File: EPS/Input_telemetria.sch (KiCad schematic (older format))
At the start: 21 parts

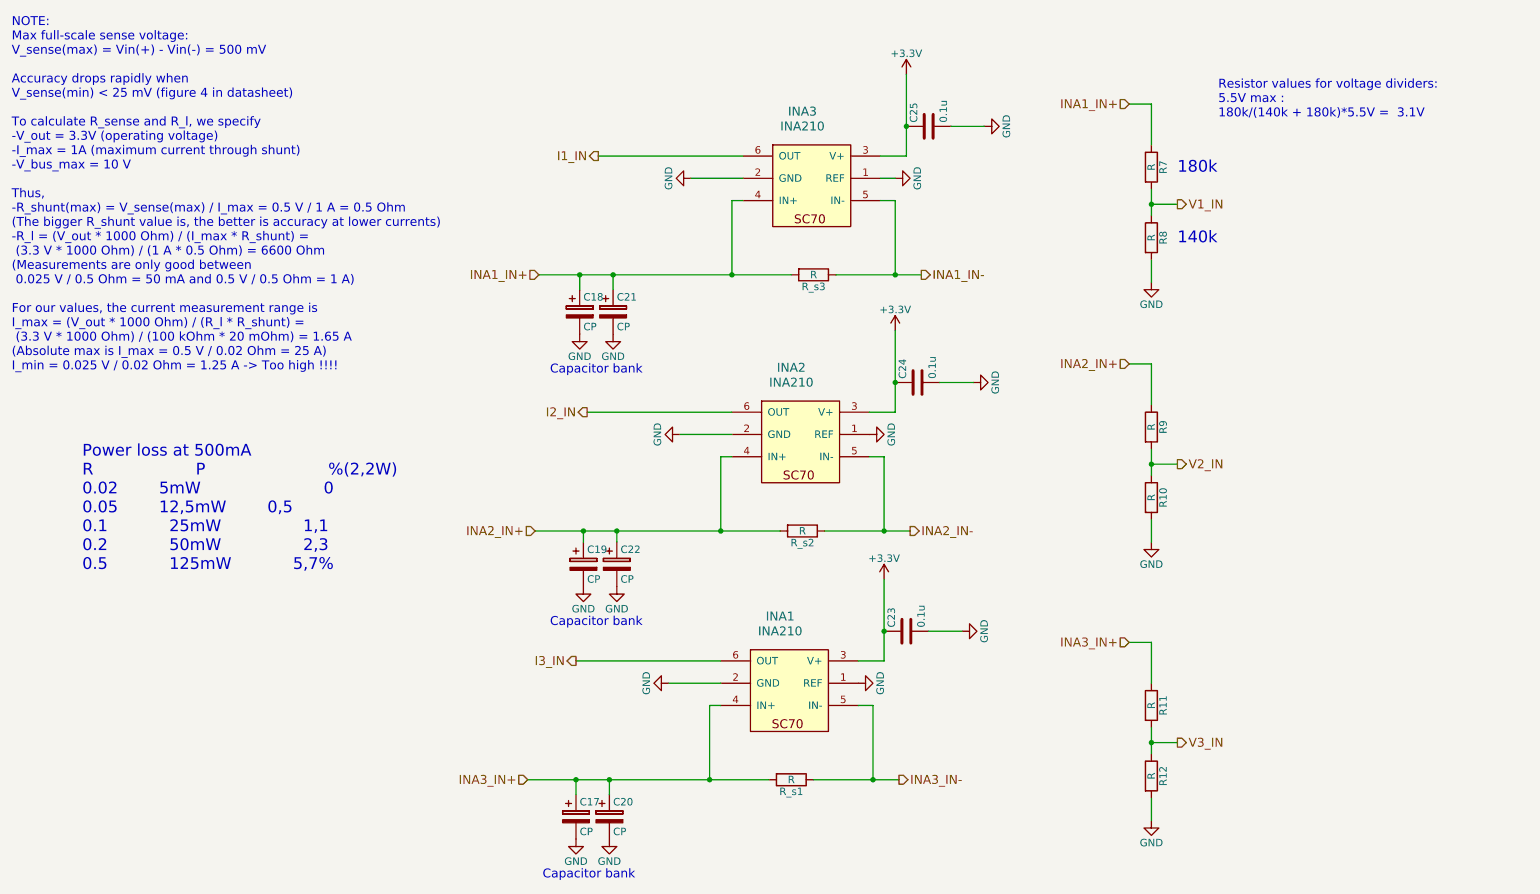
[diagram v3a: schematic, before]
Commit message: PCB updated
Added testpoints and updated PCB
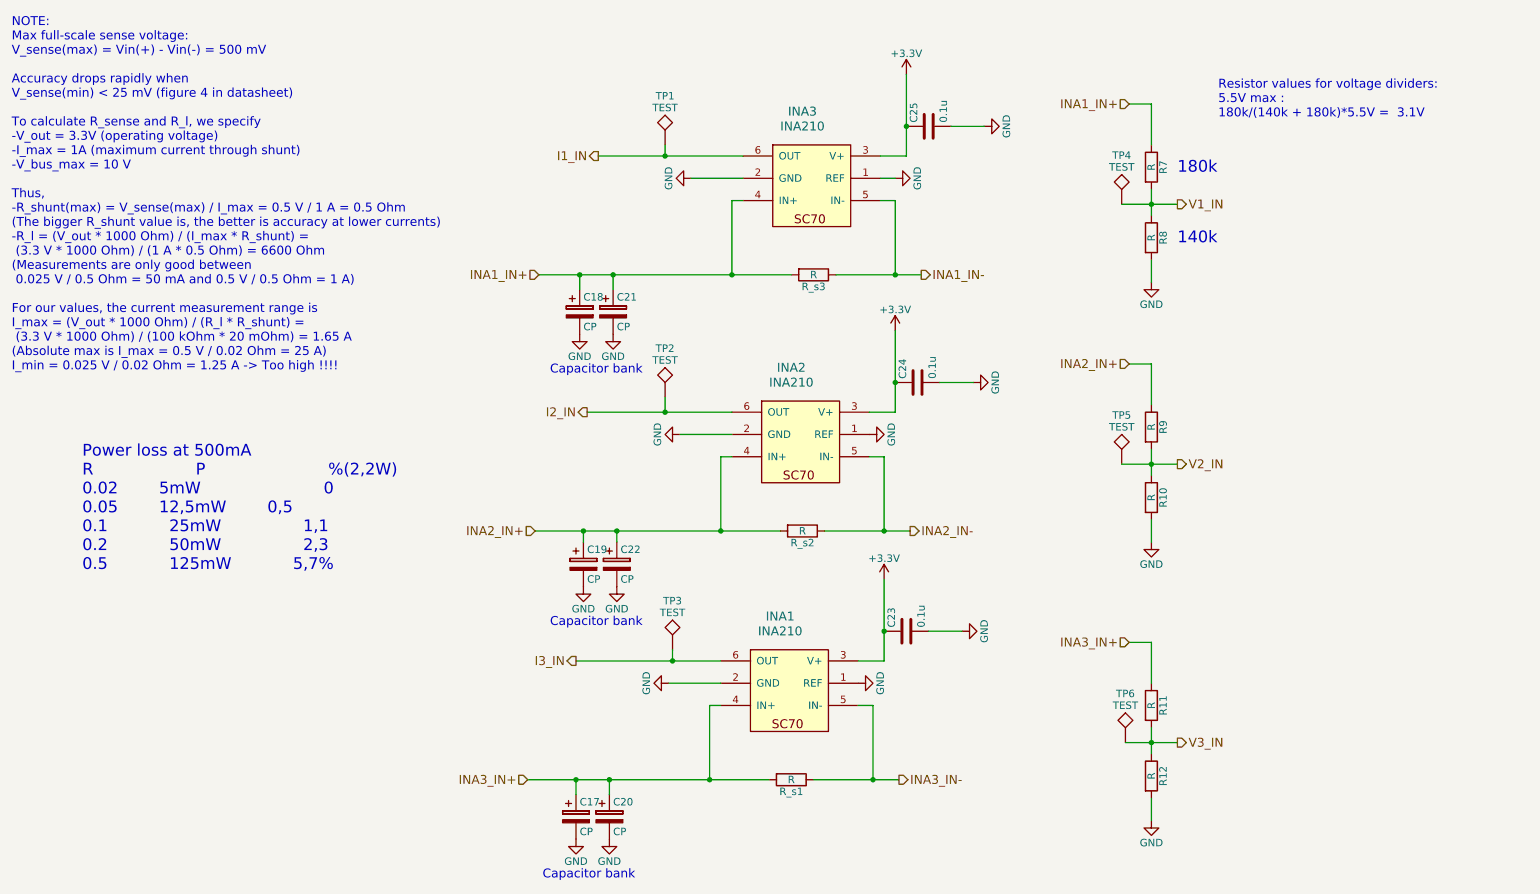
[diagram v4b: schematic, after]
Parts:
- added TP1, TP2, TP3, TP4, TP5, TP6: TEST, Measurement_Points:Measurement_Point_Round-SMD-Pad_Small, symbol TEST
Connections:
- net I1_IN: now also TP1.1
- net I2_IN: now also TP2.1
- net I3_IN: now also TP3.1
- net V1_IN: now also TP4.1
- net V2_IN: now also TP5.1
- net V3_IN: now also TP6.1
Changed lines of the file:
@@
 $EndComp
 $Comp
-L GND #PWR029
+L GND #PWR028
 U 1 1 5A8147F5
 P 5150 1650
-F 0 "#PWR029" H 5150 1400 50  0001 C CNN
+F 0 "#PWR028" H 5150 1400 50  0001 C CNN
 F 1 "GND" H 5150 1500 50  0000 C CNN
 F 2 "" H 5150 1650 50  0001 C CNN
@@
 $EndComp
 $Comp
-L +3.3V #PWR030
+L +3.3V #PWR029
 U 1 1 5A814819
 P 6600 950
-F 0 "#PWR030" H 6600 800 50  0001 C CNN
+F 0 "#PWR029" H 6600 800 50  0001 C CNN
 F 1 "+3.3V" H 6600 1090 50  0000 C CNN
 F 2 "" H 6600 950 50  0001 C CNN
@@
 Connection ~ 6600 1300
 $Comp
-L GND #PWR031
+L GND #PWR030
 U 1 1 5A814EB4
 P 7125 1300
-F 0 "#PWR031" H 7125 1050 50  0001 C CNN
+F 0 "#PWR030" H 7125 1050 50  0001 C CNN
 F 1 "GND" H 7125 1150 50  0000 C CNN
 F 2 "" H 7125 1300 50  0001 C CNN
@@
 $EndComp
 $Comp
-L GND #PWR032
+L GND #PWR031
 U 1 1 5A818451
 P 5075 3375
-F 0 "#PWR032" H 5075 3125 50  0001 C CNN
+F 0 "#PWR031" H 5075 3125 50  0001 C CNN
 F 1 "GND" H 5075 3225 50  0000 C CNN
 F 2 "" H 5075 3375 50  0001 C CNN
@@
 $EndComp
 $Comp
-L +3.3V #PWR033
+L +3.3V #PWR032
 U 1 1 5A818457
 P 6525 2675
-F 0 "#PWR033" H 6525 2525 50  0001 C CNN
+F 0 "#PWR032" H 6525 2525 50  0001 C CNN
 F 1 "+3.3V" H 6525 2815 50  0000 C CNN
 F 2 "" H 6525 2675 50  0001 C CNN
@@
 Connection ~ 6525 3025
 $Comp
-L GND #PWR034
+L GND #PWR033
 U 1 1 5A818460
 P 7050 3025
-F 0 "#PWR034" H 7050 2775 50  0001 C CNN
+F 0 "#PWR033" H 7050 2775 50  0001 C CNN
 F 1 "GND" H 7050 2875 50  0000 C CNN
 F 2 "" H 7050 3025 50  0001 C CNN
@@
 $EndComp
 $Comp
-L GND #PWR035
+L GND #PWR034
 U 1 1 5A818591
 P 5000 5050
-F 0 "#PWR035" H 5000 4800 50  0001 C CNN
+F 0 "#PWR034" H 5000 4800 50  0001 C CNN
 F 1 "GND" H 5000 4900 50  0000 C CNN
 F 2 "" H 5000 5050 50  0001 C CNN
@@
 $EndComp
 $Comp
-L +3.3V #PWR036
+L +3.3V #PWR035
 U 1 1 5A818597
 P 6450 4350
-F 0 "#PWR036" H 6450 4200 50  0001 C CNN
+F 0 "#PWR035" H 6450 4200 50  0001 C CNN
 F 1 "+3.3V" H 6450 4490 50  0000 C CNN
 F 2 "" H 6450 4350 50  0001 C CNN
@@
 Connection ~ 6450 4700
 $Comp
-L GND #PWR037
+L GND #PWR036
 U 1 1 5A8185A0
 P 6975 4700
-F 0 "#PWR037" H 6975 4450 50  0001 C CNN
+F 0 "#PWR036" H 6975 4450 50  0001 C CNN
 F 1 "GND" H 6975 4550 50  0000 C CNN
 F 2 "" H 6975 4700 50  0001 C CNN
@@
 $EndComp
 $Comp
-L GND #PWR038
+L GND #PWR037
 U 1 1 5A81C8D6
 P 8250 2350
-F 0 "#PWR038" H 8250 2100 50  0001 C CNN
+F 0 "#PWR037" H 8250 2100 50  0001 C CNN
 F 1 "GND" H 8250 2200 50  0000 C CNN
 F 2 "" H 8250 2350 50  0001 C CNN
@@
 V1_IN
 Wire Wire Line
-	8425 1825 8250 1825
+	8050 1825 8425 1825
 Connection ~ 8250 1825
 $Comp
@@
 $EndComp
 $Comp
-L GND #PWR039
+L GND #PWR038
 U 1 1 5A81D4E7
 P 8250 4100
-F 0 "#PWR039" H 8250 3850 50  0001 C CNN
+F 0 "#PWR038" H 8250 3850 50  0001 C CNN
 F 1 "GND" H 8250 3950 50  0000 C CNN
 F 2 "" H 8250 4100 50  0001 C CNN
@@
 V2_IN
 Wire Wire Line
-	8425 3575 8250 3575
+	8050 3575 8425 3575
 Connection ~ 8250 3575
 $Comp
@@
 $EndComp
 $Comp
-L GND #PWR040
+L GND #PWR039
 U 1 1 5A81E115
 P 8250 5975
-F 0 "#PWR040" H 8250 5725 50  0001 C CNN
+F 0 "#PWR039" H 8250 5725 50  0001 C CNN
 F 1 "GND" H 8250 5825 50  0000 C CNN
 F 2 "" H 8250 5975 50  0001 C CNN
@@
 V3_IN
 Wire Wire Line
-	8425 5450 8250 5450
+	8075 5450 8425 5450
 Connection ~ 8250 5450
 Text Notes 8700 1250 0    60   ~ 0
@@
 $EndComp
 $Comp
-L GND #PWR041
+L GND #PWR040
 U 1 1 5A8C57FE
 P 6525 1650
-F 0 "#PWR041" H 6525 1400 50  0001 C CNN
+F 0 "#PWR040" H 6525 1400 50  0001 C CNN
 F 1 "GND" H 6525 1500 50  0000 C CNN
 F 2 "" H 6525 1650 50  0001 C CNN
@@
 $EndComp
 $Comp
-L GND #PWR042
+L GND #PWR041
 U 1 1 5A8C5D86
 P 6350 3375
-F 0 "#PWR042" H 6350 3125 50  0001 C CNN
+F 0 "#PWR041" H 6350 3125 50  0001 C CNN
 F 1 "GND" H 6350 3225 50  0000 C CNN
 F 2 "" H 6350 3375 50  0001 C CNN
@@
 $EndComp
 $Comp
-L GND #PWR043
+L GND #PWR042
 U 1 1 5A8C5E21
 P 6275 5050
-F 0 "#PWR043" H 6275 4800 50  0001 C CNN
+F 0 "#PWR042" H 6275 4800 50  0001 C CNN
 F 1 "GND" H 6275 4900 50  0000 C CNN
 F 2 "" H 6275 5050 50  0001 C CNN
@@
 $EndComp
 $Comp
-L GND #PWR044
+L GND #PWR043
 U 1 1 5A977611
 P 4425 4400
-F 0 "#PWR044" H 4425 4150 50  0001 C CNN
+F 0 "#PWR043" H 4425 4150 50  0001 C CNN
 F 1 "GND" H 4425 4250 50  0000 C CNN
 F 2 "" H 4425 4400 50  0001 C CNN
@@
 $EndComp
 $Comp
-L GND #PWR045
+L GND #PWR044
 U 1 1 5A977718
 P 4650 4400
-F 0 "#PWR045" H 4650 4150 50  0001 C CNN
+F 0 "#PWR044" H 4650 4150 50  0001 C CNN
 F 1 "GND" H 4650 4250 50  0000 C CNN
 F 2 "" H 4650 4400 50  0001 C CNN
@@
 Connection ~ 4600 5700
 $Comp
-L GND #PWR046
+L GND #PWR045
 U 1 1 5A978EBC
 P 4375 6100
-F 0 "#PWR046" H 4375 5850 50  0001 C CNN
+F 0 "#PWR045" H 4375 5850 50  0001 C CNN
 F 1 "GND" H 4375 5950 50  0000 C CNN
 F 2 "" H 4375 6100 50  0001 C CNN
@@
 $EndComp
 $Comp
-L GND #PWR047
+L GND #PWR046
 U 1 1 5A978EC8
 P 4600 6100
-F 0 "#PWR047" H 4600 5850 50  0001 C CNN
+F 0 "#PWR046" H 4600 5850 50  0001 C CNN
 F 1 "GND" H 4600 5950 50  0000 C CNN
 F 2 "" H 4600 6100 50  0001 C CNN
@@
 Connection ~ 4650 4025
 $Comp
-L GND #PWR048
+L GND #PWR047
 U 1 1 5A979D03
 P 4400 2700
-F 0 "#PWR048" H 4400 2450 50  0001 C CNN
+F 0 "#PWR047" H 4400 2450 50  0001 C CNN
 F 1 "GND" H 4400 2550 50  0000 C CNN
 F 2 "" H 4400 2700 50  0001 C CNN
@@
 $EndComp
 $Comp
-L GND #PWR049
+L GND #PWR048
 U 1 1 5A979D0F
 P 4625 2700
-F 0 "#PWR049" H 4625 2450 50  0001 C CNN
+F 0 "#PWR048" H 4625 2450 50  0001 C CNN
 F 1 "GND" H 4625 2550 50  0000 C CNN
 F 2 "" H 4625 2700 50  0001 C CNN
@@
 	0    1    1    0
 $EndComp
+$Comp
+L TEST TP1
+U 1 1 5A9E9598
+P 4975 1425
+F 0 "TP1" H 4975 1725 50  0000 C BNN
+F 1 "TEST" H 4975 1675 50  0000 C CNN
+F 2 "Measurement_Points:Measurement_Point_Round-SMD-Pad_Small" H 4975 1425 50  0001 C CNN
+F 3 "" H 4975 1425 50  0001 C CNN
+	1    4975 1425
+	1    0    0    -1
+$EndComp
+$Comp
+L TEST TP2
+U 1 1 5A9E968D
+P 4975 3125
+F 0 "TP2" H 4975 3425 50  0000 C BNN
+F 1 "TEST" H 4975 3375 50  0000 C CNN
+F 2 "Measurement_Points:Measurement_Point_Round-SMD-Pad_Small" H 4975 3125 50  0001 C CNN
+F 3 "" H 4975 3125 50  0001 C CNN
+	1    4975 3125
+	1    0    0    -1
+$EndComp
+$Comp
+L TEST TP3
+U 1 1 5A9E96F8
+P 5025 4825
+F 0 "TP3" H 5025 5125 50  0000 C BNN
+F 1 "TEST" H 5025 5075 50  0000 C CNN
+F 2 "Measurement_Points:Measurement_Point_Round-SMD-Pad_Small" H 5025 4825 50  0001 C CNN
+F 3 "" H 5025 4825 50  0001 C CNN
+	1    5025 4825
+	1    0    0    -1
+$EndComp
+Wire Wire Line
+	5025 4900 5025 4825
+Connection ~ 5025 4900
+Wire Wire Line
+	4975 3225 4975 3125
+Connection ~ 4975 3225
+Wire Wire Line
+	4975 1500 4975 1425
+Connection ~ 4975 1500
+$Comp
+L TEST TP4
+U 1 1 5A9E9F9F
+P 8050 1825
+F 0 "TP4" H 8050 2125 50  0000 C BNN
+F 1 "TEST" H 8050 2075 50  0000 C CNN
+F 2 "Measurement_Points:Measurement_Point_Round-SMD-Pad_Small" H 8050 1825 50  0001 C CNN
+F 3 "" H 8050 1825 50  0001 C CNN
+	1    8050 1825
+	1    0    0    -1
+$EndComp
+$Comp
+L TEST TP5
+U 1 1 5A9EA085
+P 8050 3575
+F 0 "TP5" H 8050 3875 50  0000 C BNN
+F 1 "TEST" H 8050 3825 50  0000 C CNN
+F 2 "Measurement_Points:Measurement_Point_Round-SMD-Pad_Small" H 8050 3575 50  0001 C CNN
+F 3 "" H 8050 3575 50  0001 C CNN
+	1    8050 3575
+	1    0    0    -1
+$EndComp
+$Comp
+L TEST TP6
+U 1 1 5A9EA11F
+P 8075 5450
+F 0 "TP6" H 8075 5750 50  0000 C BNN
+F 1 "TEST" H 8075 5700 50  0000 C CNN
+F 2 "Measurement_Points:Measurement_Point_Round-SMD-Pad_Small" H 8075 5450 50  0001 C CNN
+F 3 "" H 8075 5450 50  0001 C CNN
+	1    8075 5450
+	1    0    0    -1
+$EndComp
 $EndSCHEMATC

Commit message: Updated PCB
PCB requires mcu to be routed.
Changed to thermistor connector on pcb
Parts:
- renumbered INA3 to INA1, INA1 to INA3
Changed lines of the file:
@@
 Power loss at 500mA\nR					P						%(2,2W)		\n0.02		5mW						0			\n0.05		12,5mW		0,5			\n0.1			25mW				1,1			\n0.2			50mW				2,3			\n0.5			125mW			5,7%
 $Comp
-L INA210 INA3
+L INA210 INA1
 U 1 1 5A8C5757
 P 5700 1425
-F 0 "INA3" H 5900 1650 60  0000 C CNN
+F 0 "INA1" H 5900 1650 60  0000 C CNN
 F 1 "INA210" H 5900 1550 60  0000 C CNN
 F 2 "TO_SOT_Packages_SMD:SOT-363_SC-70-6" H 5900 1550 60  0001 C CNN
@@
 $EndComp
 $Comp
-L INA210 INA1
+L INA210 INA3
 U 1 1 5A8C5CFE
 P 5550 4825
-F 0 "INA1" H 5750 5050 60  0000 C CNN
+F 0 "INA3" H 5750 5050 60  0000 C CNN
 F 1 "INA210" H 5750 4950 60  0000 C CNN
 F 2 "TO_SOT_Packages_SMD:SOT-363_SC-70-6" H 5750 4950 60  0001 C CNN
